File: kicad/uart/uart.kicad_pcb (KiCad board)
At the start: 2 copper layers, 160 x 100.3 mm, 19 parts, among them P1 CONN_02X05, P5 CONN_02X25, U1 16550, U2 74LS06, U3 MAX232, X1 OSC

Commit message: jumper
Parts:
- added P2: CONN_02X03, Pin_Headers:Pin_Header_Straight_2x03, F.Cu at (208.3, 108.7)
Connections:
- U1 pad 18: /WE -> Net-(P2-Pad4)
- U1 pad 21: /OE -> Net-(P2-Pad3)
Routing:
- net Net-(P2-Pad3): track 0.00 -> 71.4 mm, vias 0 -> 1
- net /OE: track 75.1 -> 9.89 mm, vias 1 -> 0
- net Net-(P2-Pad4): track 0.00 -> 59.1 mm, vias 0 -> 1
- net /WE: track 61.7 -> 9.23 mm, vias 1 -> 0
- net Net-(U1-Pad16): track 0.00 -> 30.1 mm
- net Net-(R1-Pad2): track 51.4 -> 63.0 mm
- net /WE2: track 0.00 -> 9.23 mm
- net /OE2: track 0.00 -> 9.23 mm

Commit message: layout
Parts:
- removed P1: CONN_02X05, Connect:DB9FC
- removed P2: CONN_02X03, Pin_Headers:Pin_Header_Straight_2x03
- added J1: DB9, Connect:DB9MC, F.Cu at (80.6, 94.6)
- C1, C2, C3, C4, C7: footprint Capacitors_Elko_ThroughHole:Elko_vert_DM5_RM2 -> Capacitors_Elko_ThroughHole:Elko_vert_11.2x6.3mm_RM2.5_CopperClear
- moved C5 82.3 mm to (207.6, 71.8), turned to 90 degrees
- moved C6 32.6 mm to (205.6, 102.2), turned to 270 degrees
- moved C7 31.9 mm to (109.9, 104.8), turned to 180 degrees
- moved C3 24.1 mm to (92.1, 85.1), turned to 0 degrees
- moved U1 23.8 mm to (179.1, 91.4), turned to 180 degrees
- moved U3 23.6 mm to (101.0, 95.2), turned to 180 degrees
- moved R1 23.2 mm to (200.7, 57.4), turned to 270 degrees
- moved U2 22.5 mm to (195.6, 69.2), turned to 180 degrees
- moved X1 13.7 mm to (172.7, 69.2), turned to 180 degrees
- moved C2 12.3 mm to (102.2, 85.1), turned to 180 degrees
- moved C4 8.35 mm to (114.9, 85.1), turned to 0 degrees
- moved R2 4.57 mm to (85.0, 93.5), turned to 90 degrees
- moved C1 4.26 mm to (109.9, 85.1), turned to 180 degrees
- moved MH2 1.91 mm to (215.6, 52.6)
- moved MH1 1.89 mm to (68.6, 52.8)
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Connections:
- P5 pad 10: /Connector/D4 -> (no net)
- P5 pad 11: /Connector/D3 -> (no net)
- P5 pad 12: /Connector/D2 -> (no net)
- P5 pad 13: /Connector/D1 -> (no net)
- P5 pad 14: /Connector/D0 -> (no net)
- P5 pad 15: Net-(P5-Pad15) -> (no net)
- P5 pad 16: /RW -> (no net)
- P5 pad 17: Net-(P5-Pad17) -> (no net)
- P5 pad 18: RDY -> (no net)
- P5 pad 19: Net-(P5-Pad19) -> (no net)
- P5 pad 20: /CS_RES02 -> (no net)
- P5 pad 21: E_LCD -> (no net)
- P5 pad 22: /CS_VIA -> (no net)
- P5 pad 24: /CSR_VDP -> (no net)
- P5 pad 25: /CSW_VDP -> (no net)
- P5 pad 26: /Connector/A4 -> (no net)
- P5 pad 27: /Connector/A3 -> (no net)
- P5 pad 28: /Connector/A2 -> (no net)
- P5 pad 29: /Connector/A1 -> (no net)
- P5 pad 3: /NMI -> (no net)
- P5 pad 30: /Connector/A0 -> (no net)
- P5 pad 35: PHI2 -> (no net)
- P5 pad 36: Net-(P5-Pad36) -> (no net)
- P5 pad 37: /OE2 -> (no net)
- P5 pad 38: /WE2 -> (no net)
- P5 pad 39: Net-(P5-Pad39) -> (no net)
- P5 pad 40: Net-(P5-Pad40) -> (no net)
- P5 pad 41: Net-(P5-Pad41) -> (no net)
- P5 pad 42: Net-(P5-Pad42) -> (no net)
- P5 pad 43: Net-(P5-Pad43) -> VCC
- P5 pad 44: Net-(P5-Pad44) -> VCC
- P5 pad 45: Net-(P5-Pad45) -> VCC
- P5 pad 46: Net-(P5-Pad46) -> VCC
- P5 pad 47: Net-(P5-Pad47) -> GND
- P5 pad 48: Net-(P5-Pad48) -> GND
- P5 pad 49: Net-(P5-Pad49) -> GND
- P5 pad 5: Net-(P5-Pad5) -> (no net)
- P5 pad 50: Net-(P5-Pad50) -> GND
- P5 pad 6: Net-(P5-Pad6) -> (no net)
- P5 pad 7: /Connector/D7 -> (no net)
- P5 pad 8: /Connector/D6 -> (no net)
- P5 pad 9: /Connector/D5 -> (no net)
- U1 pad 1: /Connector/D0 -> (no net)
- U1 pad 17: Net-(U1-Pad17) -> (no net)
- U1 pad 18: Net-(P2-Pad4) -> /WE
- U1 pad 2: /Connector/D1 -> (no net)
- U1 pad 21: Net-(P2-Pad3) -> /OE
- U1 pad 23: Net-(U1-Pad23) -> (no net)
- U1 pad 24: Net-(U1-Pad24) -> (no net)
- U1 pad 25: Net-(U1-Pad25) -> (no net)
- U1 pad 26: /Connector/A2 -> (no net)
- U1 pad 27: /Connector/A1 -> (no net)
- U1 pad 28: /Connector/A0 -> (no net)
- U1 pad 29: Net-(U1-Pad29) -> (no net)
- U1 pad 3: /Connector/D2 -> (no net)
- U1 pad 31: Net-(U1-Pad31) -> (no net)
- U1 pad 33: Net-(U1-Pad33) -> (no net)
- U1 pad 34: Net-(U1-Pad34) -> (no net)
- U1 pad 4: /Connector/D3 -> (no net)
- U1 pad 5: /Connector/D4 -> (no net)
- U1 pad 6: /Connector/D5 -> (no net)
- U1 pad 7: /Connector/D6 -> (no net)
- U1 pad 8: /Connector/D7 -> (no net)
- X1 pad 1: Net-(X1-Pad1) -> (no net)
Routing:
- net (no net): track 0.00 -> 368.4 mm
- net VCC: track 256.2 -> 181.4 mm, vias 0 -> 3
- net Net-(P2-Pad3): track 71.4 -> 0.00 mm, vias 1 -> 0
- net /Connector/D0: track 70.8 -> 0.00 mm
- net /Connector/D2: track 69.7 -> 0.00 mm
- net /Connector/A2: track 69.2 -> 0.00 mm
- net /Connector/D4: track 68.7 -> 0.00 mm
- net /Connector/A0: track 68.1 -> 0.00 mm
- net /Connector/D6: track 67.6 -> 0.00 mm
- net /Connector/D1: track 67.2 -> 0.00 mm
- net /Connector/D3: track 66.1 -> 0.00 mm
- net /Connector/A1: track 65.6 -> 0.00 mm
- net /Connector/D5: track 65.1 -> 0.00 mm
- net /Connector/D7: track 64.0 -> 0.00 mm
- net /WE: track 9.23 -> 72.9 mm
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- added copper zone on F.Cu, net GND
- added copper zone on F.Cu, net VCC

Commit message: beschriftung
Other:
- board text added: "Steckschwein UART Board 2015 Thomas Woinke / Marko Lauke http://www.steckschwein.de/"

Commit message: elko
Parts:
- added C8: 100µF, Capacitors_Elko_ThroughHole:Elko_vert_11.5x8mm_RM3.5, F.Cu at (216.4, 129.7)
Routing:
- net VCC: track 181.4 -> 185.0 mm
- net GND: track 188.3 -> 191.7 mm

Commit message: verschoenert
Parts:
- added G***: LOGO, Steckschwein:QRCODE, F.Cu at (81.4, 66.0)
- C3: footprint Capacitors_Elko_ThroughHole:Elko_vert_11.2x6.3mm_RM2.5_CopperClear -> Capacitors_Elko_ThroughHole:Elko_vert_11.2x6.3mm_RM2.5

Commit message: abblockkondensator
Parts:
- moved C8 10.2 mm to (209.0, 122.6)
- moved C6 4.94 mm to (207.8, 97.8), turned to 90 degrees
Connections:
- P5 pad 10: (no net) -> /Connector/D3
- P5 pad 11: (no net) -> /Connector/D2
- P5 pad 12: (no net) -> /Connector/D1
- P5 pad 13: (no net) -> /Connector/D0
- P5 pad 28: (no net) -> /Connector/A2
- P5 pad 29: (no net) -> /Connector/A1
- P5 pad 30: (no net) -> /Connector/A0
- P5 pad 6: (no net) -> /Connector/D7
- P5 pad 7: (no net) -> /Connector/D6
- P5 pad 8: (no net) -> /Connector/D5
- P5 pad 9: (no net) -> /Connector/D4
- U1 pad 1: (no net) -> /Connector/D0
- U1 pad 2: (no net) -> /Connector/D1
- U1 pad 26: (no net) -> /Connector/A2
- U1 pad 27: (no net) -> /Connector/A1
- U1 pad 28: (no net) -> /Connector/A0
- U1 pad 3: (no net) -> /Connector/D2
- U1 pad 4: (no net) -> /Connector/D3
- U1 pad 5: (no net) -> /Connector/D4
- U1 pad 6: (no net) -> /Connector/D5
- U1 pad 7: (no net) -> /Connector/D6
- U1 pad 8: (no net) -> /Connector/D7
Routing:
- net (no net): track 368.4 -> 0.00 mm
- net /Connector/A2: track 0.00 -> 54.0 mm
- net /Connector/A1: track 0.00 -> 47.7 mm
- net /Connector/A0: track 0.00 -> 47.1 mm
- net GND: track 191.7 -> 237.7 mm, vias 0 -> 1
- net /Connector/D7: track 0.00 -> 37.9 mm
- net /Connector/D5: track 0.00 -> 31.8 mm
- net /Connector/D6: track 0.00 -> 31.8 mm
- net /Connector/D3: track 0.00 -> 25.9 mm
- net /Connector/D4: track 0.00 -> 25.6 mm
- net /Connector/D1: track 0.00 -> 19.5 mm
- net /Connector/D2: track 0.00 -> 19.5 mm
- net /Connector/D0: track 0.00 -> 14.3 mm
- net VCC: track 185.0 -> 183.0 mm, vias 3 -> 2

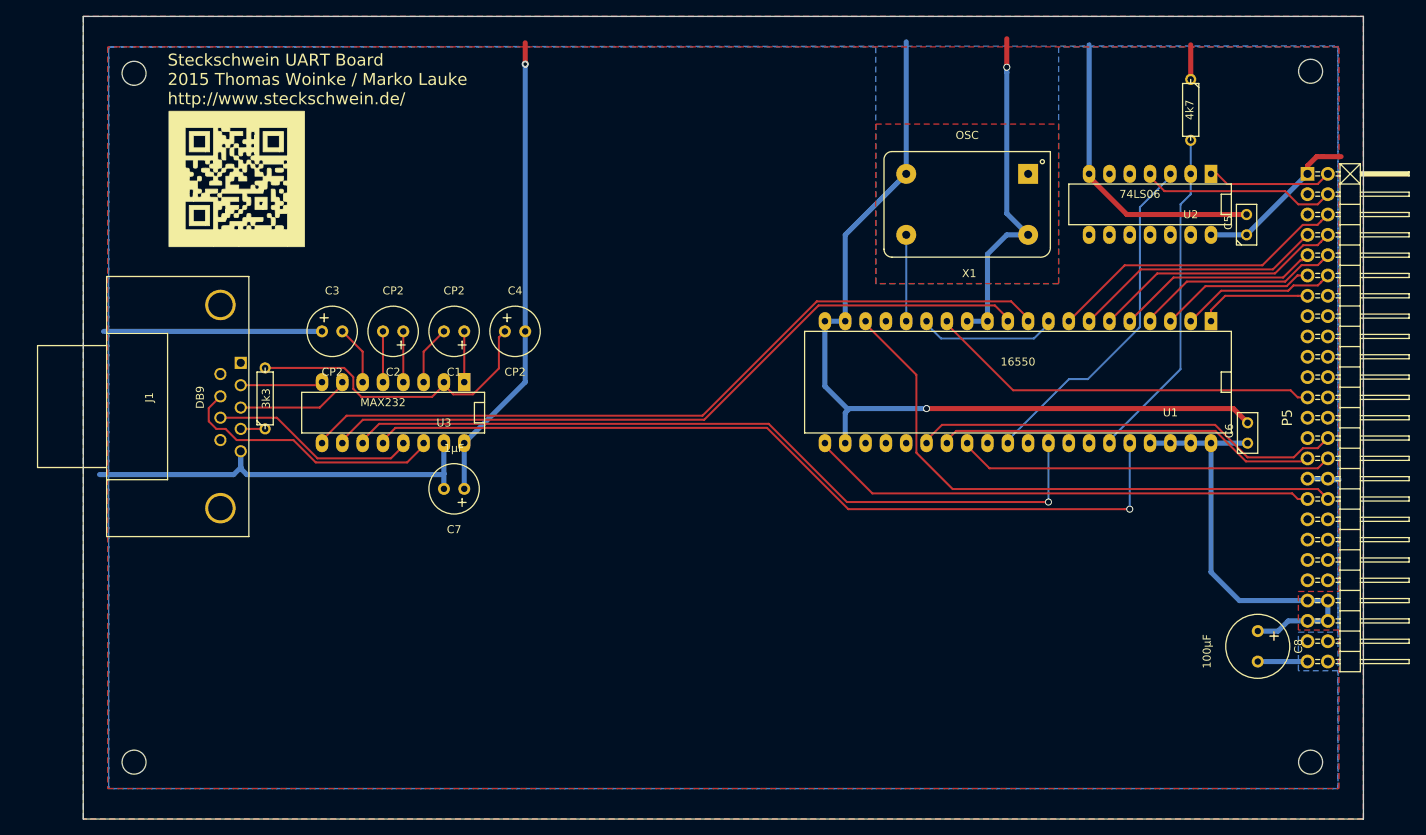
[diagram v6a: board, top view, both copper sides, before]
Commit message: dsub footprint
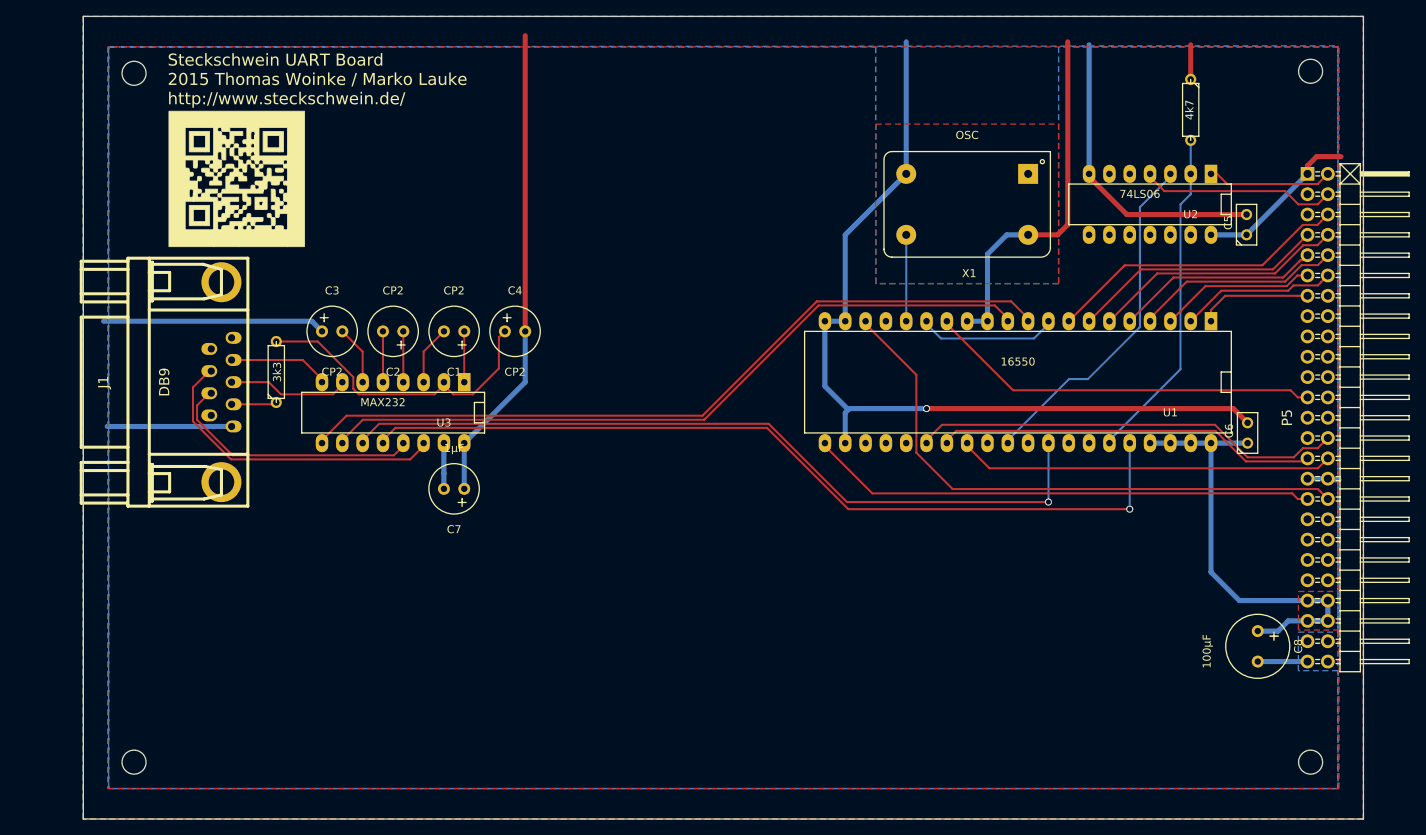
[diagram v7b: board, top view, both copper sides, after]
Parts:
- C3: footprint Capacitors_Elko_ThroughHole:Elko_vert_11.2x6.3mm_RM2.5 -> Capacitors_Elko_ThroughHole:Elko_vert_11.2x6.3mm_RM2.5_CopperClear
- J1: footprint Connect:DB9MC -> DSUB:DB_9M
- moved J1 8.84 mm to (72.4, 91.4), turned to 270 degrees
- moved R2 3.59 mm to (86.4, 90.2)
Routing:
- net GND: track 237.7 -> 205.8 mm
- net Net-(J1-Pad8): track 26.3 -> 33.0 mm
- net Net-(J1-Pad7): track 33.9 -> 39.2 mm
- net VCC: track 183.0 -> 186.6 mm, vias 2 -> 0
- net Net-(J1-Pad2): track 10.3 -> 13.8 mm
- net Net-(J1-Pad4): track 3.05 -> 5.68 mm
- net Net-(J1-Pad3): track 14.2 -> 15.3 mm

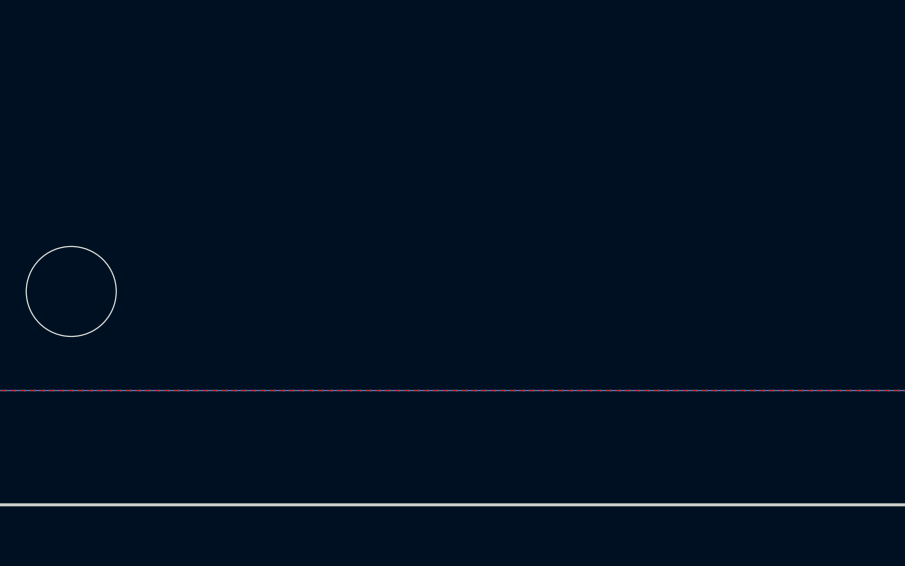
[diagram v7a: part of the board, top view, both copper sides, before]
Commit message: 3d models, layer label
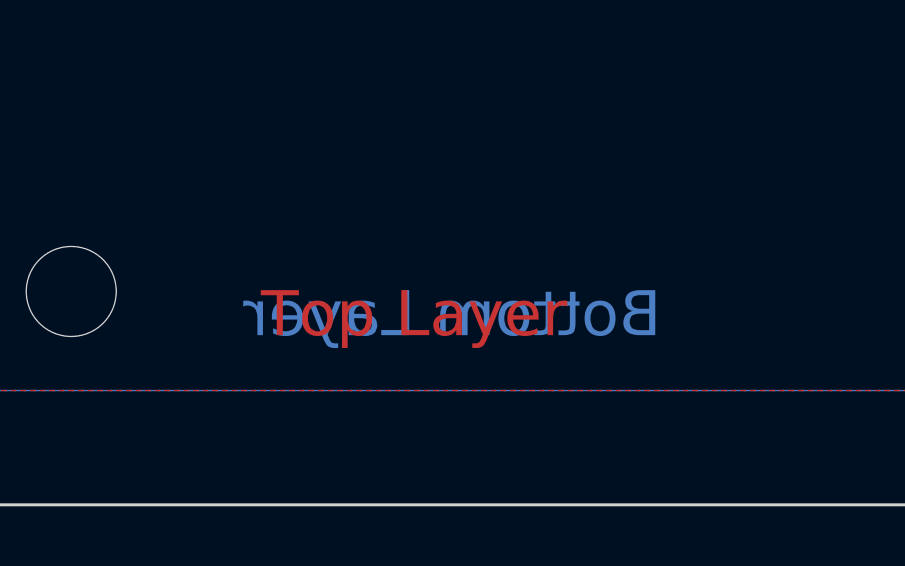
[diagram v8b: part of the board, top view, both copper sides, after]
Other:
- board text added: "Bottom Layer"
- board text added: "Top Layer"
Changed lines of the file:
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@@
     (links 73)
     (no_connects 0)
-    (area 62.179999 45.669999 222.300001 146.100001)
+    (area 45.516073 45.669999 240.711447 146.100001)
     (thickness 1.6)
-    (drawings 5)
+    (drawings 7)
     (tracks 242)
     (zones 0)
@@
       (layerselection 0x00020_80000001)
       (usegerberextensions false)
+      (usegerberattributes true)
       (excludeedgelayer true)
       (linewidth 0.100000)
@@
     (pad 40 thru_hole oval (at -24.13 -7.62 180) (size 1.5748 2.286) (drill 0.8128) (layers *.Cu *.Mask F.SilkS)
       (net 2 VCC))
-    (model dil/sockets/dil_socket_40_600.wrl
+    (model ../../../../../../home/thomas/Documents/steckschwein/kicad/lbr/3d/walter/pth_circuits/dil_40-600_socket.wrl
       (at (xyz 0 0 0))
       (scale (xyz 1 1 1))
@@
     (pad 14 thru_hole oval (at -7.62 -3.81 180) (size 1.5748 2.286) (drill 0.8128) (layers *.Cu *.Mask F.SilkS)
       (net 2 VCC))
-    (model dil/dil_14.wrl
+    (model ../../../../../../home/thomas/Documents/steckschwein/kicad/lbr/3d/walter/pth_circuits/dil_14-300_socket.wrl
       (at (xyz 0 0 0))
       (scale (xyz 1 1 1))
@@
     (pad 16 thru_hole oval (at -8.89 -3.81 180) (size 1.5748 2.286) (drill 0.8128) (layers *.Cu *.Mask F.SilkS)
       (net 2 VCC))
-    (model dil/dil_16.wrl
+    (model ../../../../../../home/thomas/Documents/steckschwein/kicad/lbr/3d/walter/pth_circuits/dil_16-300_socket.wrl
       (at (xyz 0 0 0))
       (scale (xyz 1 1 1))
@@
     (pad 1 thru_hole circle (at 0 0) (size 1.50114 1.50114) (drill 0.8001) (layers *.Cu *.Mask F.SilkS)
       (net 1 GND))
-    (model Capacitors_Elko_ThroughHole/Elko_vert_11.2x6.3mm_RM2.5_CopperClear.wrl
+    (model Capacitors_Electrolytic/Cap_11x5mm_RM2.5.wrl
       (at (xyz 0 0 0))
       (scale (xyz 1 1 1))
@@
     )
   )
+  (gr_text "Bottom Layer" (at 81.28 139.7) (layer B.Cu)
+    (effects (font (size 1.5 1.5) (thickness 0.3)) (justify mirror))
+  )
+  (gr_text "Top Layer" (at 80.01 139.7) (layer F.Cu)
+    (effects (font (size 1.5 1.5) (thickness 0.3)))
+  )
   (gr_text "Steckschwein UART Board\n2015 Thomas Woinke / Marko Lauke\nhttp://www.steckschwein.de/" (at 72.771 53.594) (layer F.SilkS)
